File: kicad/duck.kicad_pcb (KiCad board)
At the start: 2 copper layers, 175 x 120 mm, 98 parts, among them J1 AudioJack2, J2 AudioJack2, J3 Barrel_Jack, U1 TL074, U2 TL074, U3 TL074, U4 TL074, U5 TL074, U6 TL074, U7 LM13700

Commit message: board updated with improved quack
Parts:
- R30, R32: value 10k -> 1.5k
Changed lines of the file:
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@@
 			)
 		)
-		(property "Value" "10k"
+		(property "Value" "1.5k"
 			(at 1.27 2.37 0)
 			(layer "F.Fab")
@@
 			)
 		)
-		(property "Value" "10k"
+		(property "Value" "1.5k"
 			(at 1.27 2.37 0)
 			(layer "F.Fab")

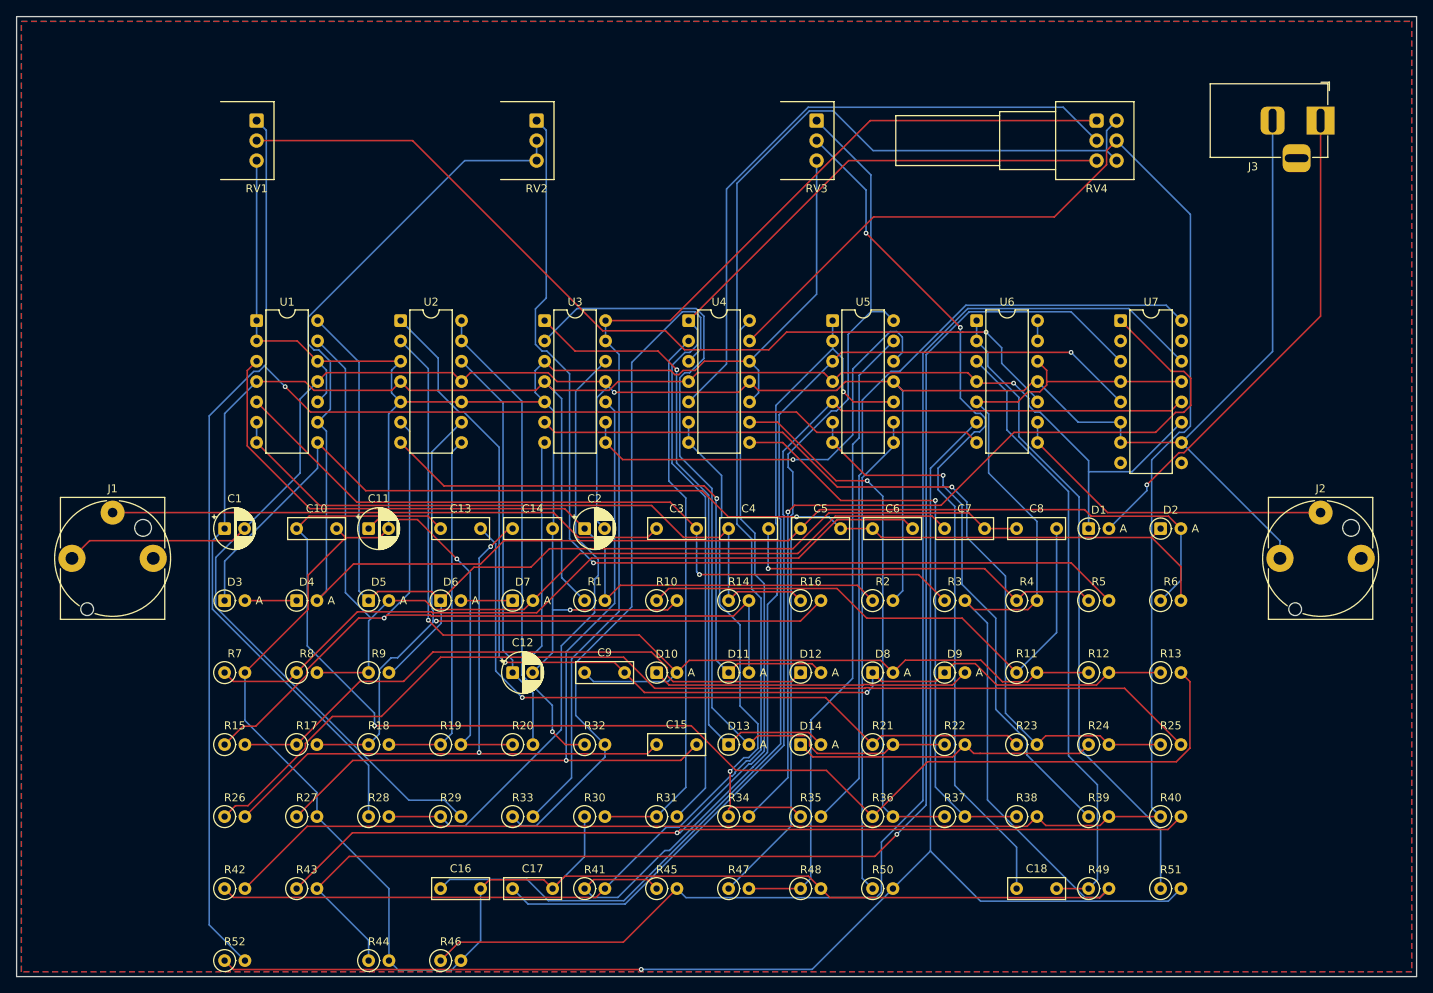
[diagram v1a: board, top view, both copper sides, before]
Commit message: audited and correct pcb design, updated breadboard instructions
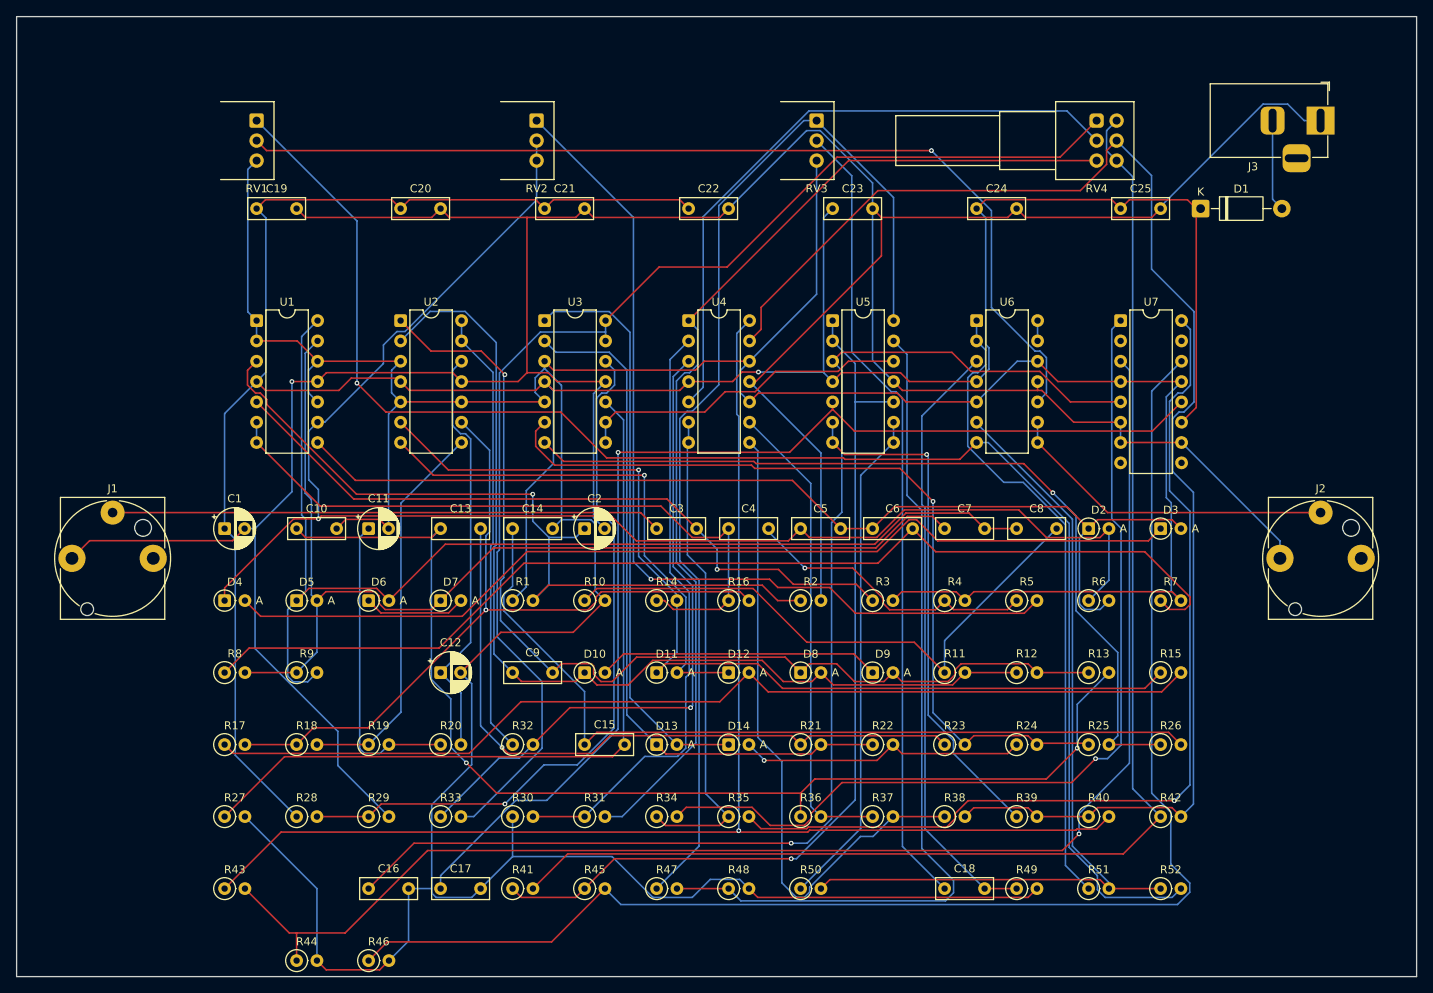
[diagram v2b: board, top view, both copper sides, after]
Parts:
- added C19: 100n, C_Rect_L7.0mm_W2.5mm_P5.00mm, F.Cu at (30.0, 24.0)
- added C20: 100n, C_Rect_L7.0mm_W2.5mm_P5.00mm, F.Cu at (48.0, 24.0)
- added C21: 100n, C_Rect_L7.0mm_W2.5mm_P5.00mm, F.Cu at (66.0, 24.0)
- added C22: 100n, C_Rect_L7.0mm_W2.5mm_P5.00mm, F.Cu at (84.0, 24.0)
- added C23: 100n, C_Rect_L7.0mm_W2.5mm_P5.00mm, F.Cu at (102.0, 24.0)
- added C24: 100n, C_Rect_L7.0mm_W2.5mm_P5.00mm, F.Cu at (120.0, 24.0)
- added C25: 100n, C_Rect_L7.0mm_W2.5mm_P5.00mm, F.Cu at (138.0, 24.0)
- D1: value 1N4148 -> 1N5817; footprint D_DO-35_SOD27_P2.54mm_Vertical_AnodeUp -> D_DO-41_SOD81_P10.16mm_Horizontal
- moved D3 117.3 mm to (143.0, 64.0)
- moved R15 117.3 mm to (143.0, 82.0)
- moved R26 117.3 mm to (143.0, 91.0)
- moved R42 117.3 mm to (143.0, 100.0)
- moved R52 117.3 mm to (143.0, 109.0)
- moved R7 117.3 mm to (143.0, 73.0)
- moved D1 42.4 mm to (148.0, 24.0)
- moved C12 9.00 mm to (53.0, 82.0)
- moved C15 9.00 mm to (71.0, 91.0)
- moved C16 9.00 mm to (44.0, 109.0)
- moved C17 9.00 mm to (53.0, 109.0)
- moved C18 9.00 mm to (116.0, 109.0)
- moved C9 9.00 mm to (62.0, 82.0)
- moved D10 9.00 mm to (71.0, 82.0)
- moved D11 9.00 mm to (80.0, 82.0)
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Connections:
- D10 pad 1: N$13 -> N$11
- D10 pad 2: N$11 -> N$13
- D11 pad 1: N$17 -> N$14
- D11 pad 2: N$14 -> N$17
- D12 pad 1: N$16 -> N$17
- D12 pad 2: N$17 -> N$16
- D13 pad 1: N$25 -> N$22
- D13 pad 2: N$22 -> N$25
- D14 pad 1: N$24 -> N$25
- D14 pad 2: N$25 -> N$24
- D3 pad 1: FZ1 -> N$5
- D3 pad 2: N$5 -> FZ1
- D4 pad 1: N$5 -> N$3
- D4 pad 2: N$3 -> N$5
- D6 pad 1: FZ2 -> N$9
- D6 pad 2: N$9 -> FZ2
- D7 pad 1: N$9 -> N$7
- D7 pad 2: N$7 -> N$9
- D9 pad 1: FZ3 -> N$13
- D9 pad 2: N$13 -> FZ3
- J3 pad 1: VRAW -> GND
- J3 pad 2: GND -> VRAW
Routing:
- net VCC: track 230.1 -> 365.2 mm
- net GND: track 327.4 -> 459.5 mm
- net N$5: track 6.46 -> 122.0 mm
- net N$35: track 267.6 -> 179.4 mm
- net N$46: track 185.4 -> 108.5 mm, vias 1 -> 0
- net N$21: track 160.3 -> 107.9 mm
- net VRAW: track 62.3 -> 11.5 mm, vias 1 -> 0
- net N$16: track 76.8 -> 126.2 mm
- net N$6: track 95.4 -> 137.0 mm
- net N$36: track 205.3 -> 172.5 mm
- net N$43: track 79.7 -> 107.7 mm
- net N$42: track 110.3 -> 136.6 mm
- net FZ: track 168.1 -> 144.8 mm, vias 1 -> 2
- net N$26: track 85.4 -> 107.5 mm, vias 2 -> 0
- net N$32: track 99.8 -> 119.4 mm, vias 0 -> 1
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- removed copper zone on B.Cu, net GND
- removed copper zone on F.Cu, net GND
